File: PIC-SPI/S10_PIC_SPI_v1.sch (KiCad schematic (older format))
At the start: 175 parts, among them P1 M25P80 ISP, P10 CONN_4, P19 XILINX CABLE2, P2 CONN_4, P3 CONN_2, P4 S100_MALE, P5 PIC_ISP, P6 CONN_1, P7 CONN_1, P8 CONN_2, P9 CONN_2, Q1 ^^NPN-SOT23, Q2 ^^NPN-SOT23, Q9 ^^NPN-SOT23, SW1 RESET, SW2 RESET, SW4 FLASH_SELECT, SW50 FLASH/RUN, U1 LDO_REG_7805, U12 ^^74LV244, U14 M25P80, U15 M25P80, U16 M25P80, U17 M25P80, U18 CH341A, U19 ^^74LS541, U2 LM1086CS, U20 XC95288XL-TQ144, U3din1 ^^74HC541, U3dout1 ^^74HC541, U4 ^^74LS541, U5 ^^74LS541, U6 ^^74LS541, U8 PIC18F1330, X1 12MHz

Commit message: PIC-SPI: annotate, add 7-segment displays (2x 74HC4511), read netlist into the PCB
Source: S100 PIC_SPI_v1/backups/06-01-2016 1810
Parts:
- removed BAR? (x2): DOT-BAR, 20dip300, symbol DOT-BAR
- removed D6: DONE, symbol LED
- removed IC? (x4), U? (x2): 74LS06N, 14dip300, symbol 74LS06N
- removed JP5: JUMPER, PIN_ARRAY_2X1, symbol JUMPER
- removed P3: CONN_2, ~, symbol CONN_2
- removed P?: MCP_1_2, symbol CONN_10X2
- removed P?: CONN_6, SIL-6, symbol CONN_6
- removed P?: CONN_3, SIL-3, symbol CONN_3
- removed Q9: ^^NPN-SOT23, ~, symbol ^^NPN-SOT23
- removed R45, R?: 330, symbol R
- removed R47: 470, symbol R
- removed RR?: 220, r_pack9, symbol RR9
- removed RR?: 4700, r_pack9, symbol RR9
- removed RR?: 470, r_pack9, symbol RR9
- removed RR?: 1000, r_pack9, symbol RR9
- removed SW4: FLASH_SELECT, symbol SW_PUSH
- removed U? (x2): 74LS20, 14dip300, symbol 74LS20
- removed U? (x2): 74LS14, 14dip300, symbol 74LS14
- removed U? (x2): 74LS08, 14dip300, symbol 74LS08
- removed U? (x8): 74LS32, 14dip300, symbol 74LS32
- added BAT1: CR2032, ~, symbol BATTERY
- added C13: 0.01 uF, symbol C
- added C16, C22, C23, C24, C29, C30, C31, C32, C41, C42, C43: 0.1 uF, symbol C
- added P11: CONN_3X2, ~, symbol CONN_3X2
- added P13: MCP_1, symbol CONN_10
- added P14: MCP_2, symbol CONN_10
- added R31, R32, R33, R34, R35, R36, R37, R38, R39, R40, R41, R42, R43, R44, R6: 1K, symbol R
- added S1, S2: 7SEGM, ~, symbol 7SEGM
- added U27, U28: 74HC4511, symbol 74HC4511
- added unit 2 of U30
- added unit 3 of U30
- D10: value FLASH_1 -> D1
- D11: value FLASH_2 -> D4
- D12: value FLASH_3 -> D5
- D2: value P55 -> D2
- D3: value P54 -> D3
- D9: value FLASH_0 -> D0
- R11: value 10k -> 1K
- U2: footprint (none) -> ~
- gave numbers to parts that had none: 26
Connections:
- net labels added: 7SEG_0_D0, 7SEG_0_D1, 7SEG_0_D2, 7SEG_0_D3, 7SEG_1_D0, 7SEG_1_D1, 7SEG_1_D2, 7SEG_1_D3, BOARD_INTERRUPT_VECTb, LED_D0, LED_D1, LED_D4, LED_D5, in8259CS*, out8259CS*, out8259CS*bufferedViaU31, sXTRQ*b
- net labels removed: BOARD_INTERRUPT_VECTc, CLK, CPLD_110, CPLD_111, CPLD_112, CPLD_113, CPLD_115, CPLD_116, CPLD_117, CPLD_118, CPLD_119, CPLD_120, CPLD_121, CPLD_124, CPLD_125, CPLD_126, CPLD_128, CPLD_129, CPLD_23, CPLD_4, CPLD_5, CPLD_66, CPLD_68, CPLD_70, CPLD_71, CPLD_72, CPLD_74, CPLD_75, CPLD_76, CPLD_77, CPLD_78, CPLD_81, FLASH_0, FLASH_1, FLASH_2, FLASH_3, MCP1_CS, MCP2_CS, PU1K-A, PU1K-AA, PU1K-B, PU1K-BB, PU1K-C, PU1K-CC, PU1K-D, PU1K-DD, PU1K-E, PU1K-EE, PU1K-F, PU1K-FF, PU1K-G, PU1K-GG, PU1K-H, PU1K-HH, PU1K-I, PU1K-II, PU1K-J, PU1K-JJ, PU1K-K, PU1K-L, PU1K-M, PU1K-N, PU1K-O, PU1K-P, PU1K-Q, PU1K-R, PU1K-S, PU1K-T, PU1K-U, PU1K-V, PU1K-W, PU1K-X, PU1K-Y, PU1K-Z, SPI_S0, SPI_SCK, SPI_SEL_0, SPI_SEL_1, SPI_SEL_2, SPI_SEL_3, SPI_SI, bA1, bA2, bA3, bA4, bA5, bA6, bA7
- wire segments 1313 -> 1268
- no-connect marks 47 -> 21
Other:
- note added: "8259 PIC"
- note added: "Active Low \npDBIN*b (READ STROBE)"
- note added: "Toshiba TC74HC4511AF(F), Decoder, Driver, Non-Inverting, 2 → 6 V, 16-Pin SOP\nRS Stock No.541-9320\n"
- note added: "to CPLD"
- note added: "to MCP2308 #1"
- note added: "to MCP2308 #2"
- note added: "to RTC DS1305"
- note removed: "/WAIT is output from slave to Processor"
- note removed: "ALL TMA lines are high when Z80 \nis Bus master"
- note removed: "Active High (All TMA lines High)\n"
- note removed: "Active High (SINTA and Read and All TMA Lines high (Z80))\n"
- note removed: "Active High (SINTA and Read)\n"
- note removed: "Active Low - pDBIN**b"
- note removed: "Active Low - pDBIN*b"
- note removed: "Active Low - sINTA*b"
- note removed: "Active Low \nAddress input with I/O req"
- note removed: "Active Low\nThis board data output, CPU data input"
- note removed: "DONE"
- note removed: "Input - from U35"
- note removed: "Pin 72 (controld run/WAIT state of processor) Input"
- note removed: "SPARES"
- note removed: "WAIT to PIN 72 S100"
- note removed: "to FPGA"
- note removed: "to LED D2"
- note removed: "to LED D3"
- note removed: "to LED's"
- note removed: "to U13"
- note removed: "to U35"
- note removed: "to U36"
- note removed: "to U37"
- note removed: "to U42"
- note removed: "to U44"
- note removed: "xxxx"
- moved on the sheet: C1, C11, C12, C14, C17, C2, C20, C21, C25, C27, C28, C3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

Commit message: PIC-SPI: add CPLD I/O header P2 and EXT SPI header P3, drop debug LEDs; placement
Source: S100 PIC_SPI_v1/backups/07-01-2016 1914
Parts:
- removed D10: D1, symbol LED
- removed D11: D4, symbol LED
- removed D12: D5, symbol LED
- removed D2: D2, symbol LED
- removed D3: D3, symbol LED
- removed P10, P2: CONN_4, symbol CONN_4
- removed R13, R16, R22, R23, R24: 330, symbol R
- added P2: CONN_8X2, symbol CONN_8X2
- added P3: EXT SPI, ~, symbol CONN_4X2
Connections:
- net labels added: CPLD_110, CPLD_111, CPLD_112, CPLD_113, CPLD_115, CPLD_116, CPLD_68, CPLD_71, CPLD_74, CPLD_75, CPLD_76, CPLD_77, CPLD_78, Vbat
- net labels removed: LED_D0, LED_D1, LED_D2, LED_D3, LED_D4, LED_D5
- wire segments 1268 -> 1271
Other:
- note added: "to EXTERNAL SPI header"
- note removed: "from U7b"
- note removed: "to U"
- moved on the sheet: C22, C30, C32

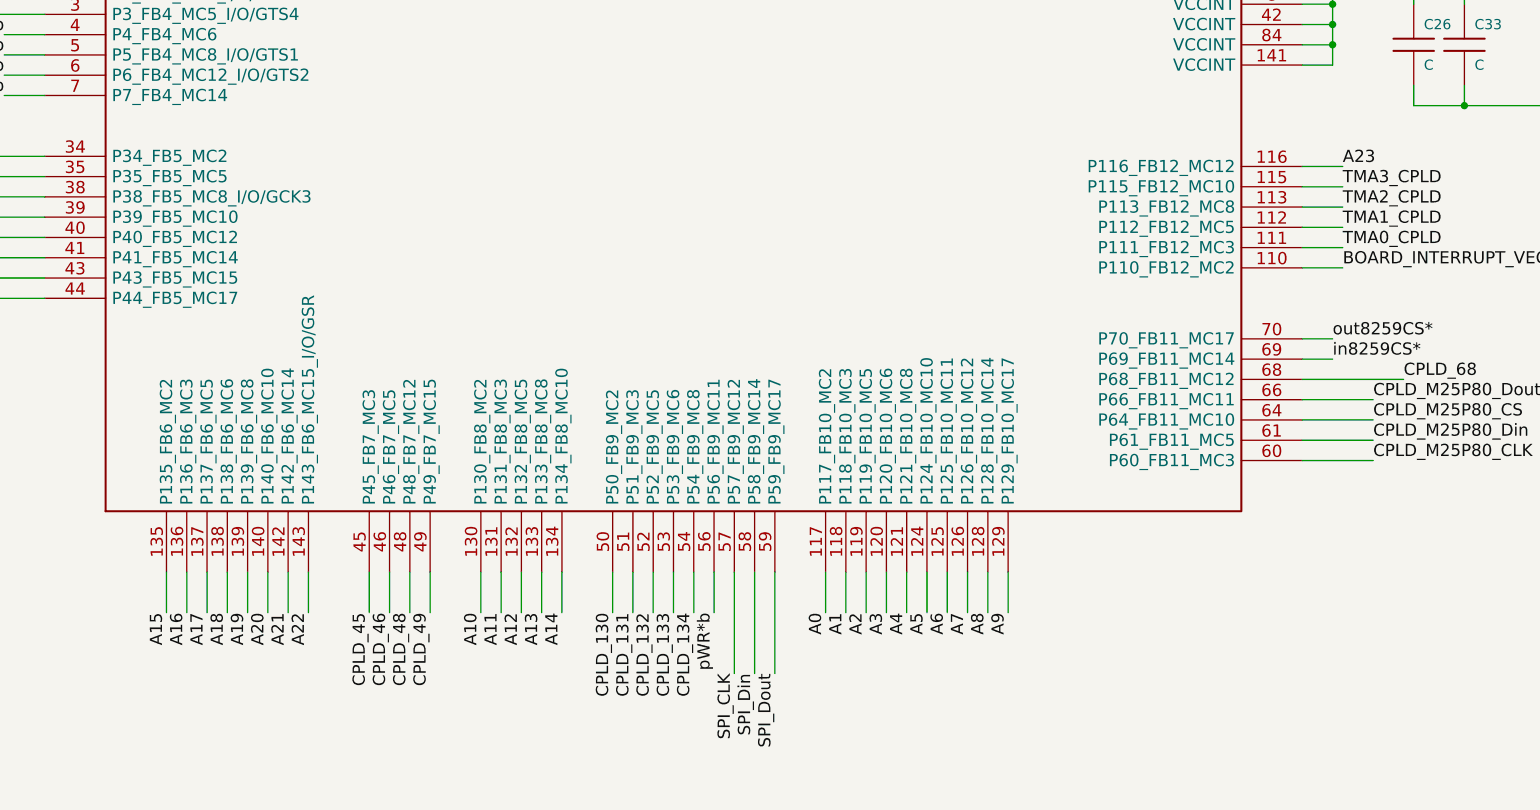
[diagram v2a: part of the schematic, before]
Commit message: PIC-SPI: rip up tracks for a reroute
Source: S100 PIC_SPI_v1/backups/09-01-2016 1434 reroute
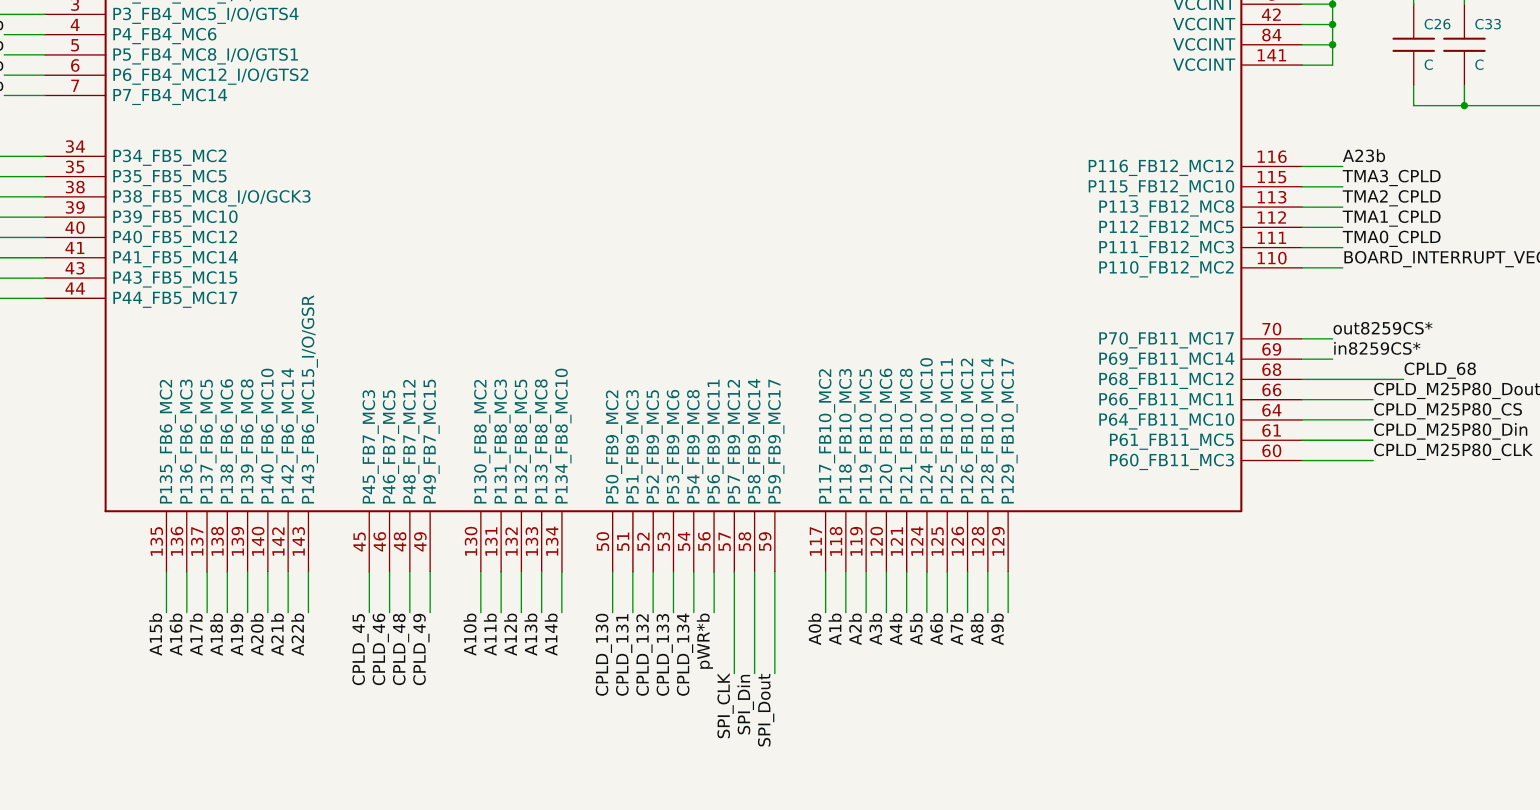
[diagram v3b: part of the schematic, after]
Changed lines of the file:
@@
 Sheet 1 1
 Title "noname.sch"
-Date "7 jan 2016"
+Date "9 jan 2016"
 Rev ""
 Comp ""
@@
 	1    0    0    -1
 $EndComp
-Text Label 30600 26550 3    60   ~ 0
-A0
-Text Label 30700 26550 3    60   ~ 0
-A1
-Text Label 30800 26550 3    60   ~ 0
-A2
-Text Label 30900 26550 3    60   ~ 0
-A3
-Text Label 31000 26550 3    60   ~ 0
-A4
-Text Label 31100 26550 3    60   ~ 0
-A5
-Text Label 31200 26550 3    60   ~ 0
-A6
-Text Label 31300 26550 3    60   ~ 0
-A7
-Text Label 31400 26550 3    60   ~ 0
-A8
-Text Label 31500 26550 3    60   ~ 0
-A9
-Text Label 28900 26550 3    60   ~ 0
-A10
-Text Label 29000 26550 3    60   ~ 0
-A11
-Text Label 29100 26550 3    60   ~ 0
-A12
-Text Label 29200 26550 3    60   ~ 0
-A13
-Text Label 29300 26550 3    60   ~ 0
-A14
-Text Label 27350 26550 3    60   ~ 0
-A15
 Text Label 33200 22350 0    60   ~ 0
 GND
@@
 Text Label 26250 20750 2    60   ~ 0
 DBUSOUT_EN
-Text Label 27650 26550 3    60   ~ 0
-A18
-Text Label 27550 26550 3    60   ~ 0
-A17
-Text Label 27450 26550 3    60   ~ 0
-A16
-Text Label 27750 26550 3    60   ~ 0
-A19
-Text Label 27850 26550 3    60   ~ 0
-A20
-Text Label 27950 26550 3    60   ~ 0
-A21
-Text Label 28050 26550 3    60   ~ 0
-A22
-Text Label 33150 24350 0    60   ~ 0
-A23
 Wire Wire Line
 	27450 26550 27450 26350
@@
 Wire Wire Line
 	32950 25800 33300 25800
+Text Label 27550 26550 3    60   ~ 0
+A17b
+Text Label 27450 26550 3    60   ~ 0
+A16b
+Text Label 27650 26550 3    60   ~ 0
+A18b
+Text Label 28900 26550 3    60   ~ 0
+A10b
+Text Label 31500 26550 3    60   ~ 0
+A9b
+Text Label 29100 26550 3    60   ~ 0
+A12b
+Text Label 27350 26550 3    60   ~ 0
+A15b
+Text Label 30900 26550 3    60   ~ 0
+A3b
+Text Label 31000 26550 3    60   ~ 0
+A4b
+Text Label 31100 26550 3    60   ~ 0
+A5b
+Text Label 29000 26550 3    60   ~ 0
+A11b
+Text Label 29300 26550 3    60   ~ 0
+A14b
+Text Label 29200 26550 3    60   ~ 0
+A13b
+Text Label 31400 26550 3    60   ~ 0
+A8b
+Text Label 31300 26550 3    60   ~ 0
+A7b
+Text Label 31200 26550 3    60   ~ 0
+A6b
+Text Label 30800 26550 3    60   ~ 0
+A2b
+Text Label 30700 26550 3    60   ~ 0
+A1b
+Text Label 30600 26550 3    60   ~ 0
+A0b
+Text Label 27750 26550 3    60   ~ 0
+A19b
+Text Label 27850 26550 3    60   ~ 0
+A20b
+Text Label 27950 26550 3    60   ~ 0
+A21b
+Text Label 28050 26550 3    60   ~ 0
+A22b
+Text Label 33150 24350 0    60   ~ 0
+A23b
 $EndSCHEMATC

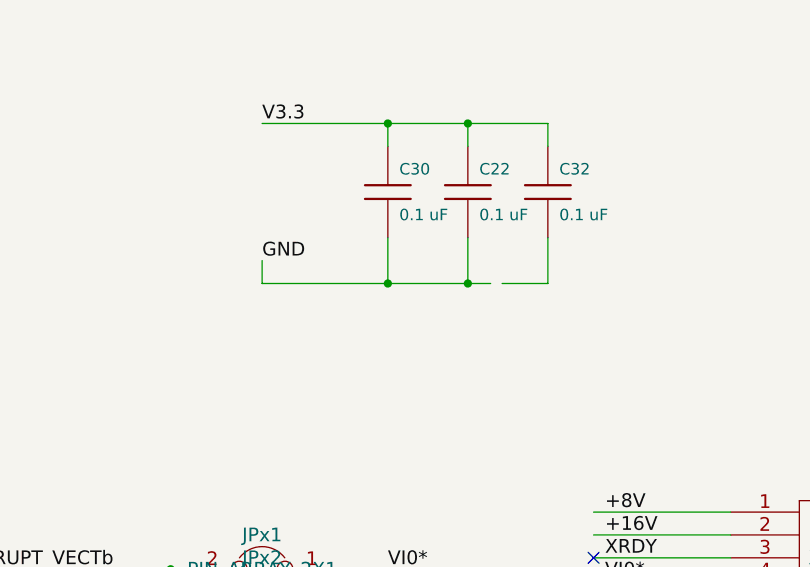
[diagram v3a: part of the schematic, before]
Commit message: PIC-SPI: schematic wiring fix, pre-route tracks before autorouting
Source: S100 PIC_SPI_v1/backups/09-01-2016 1545
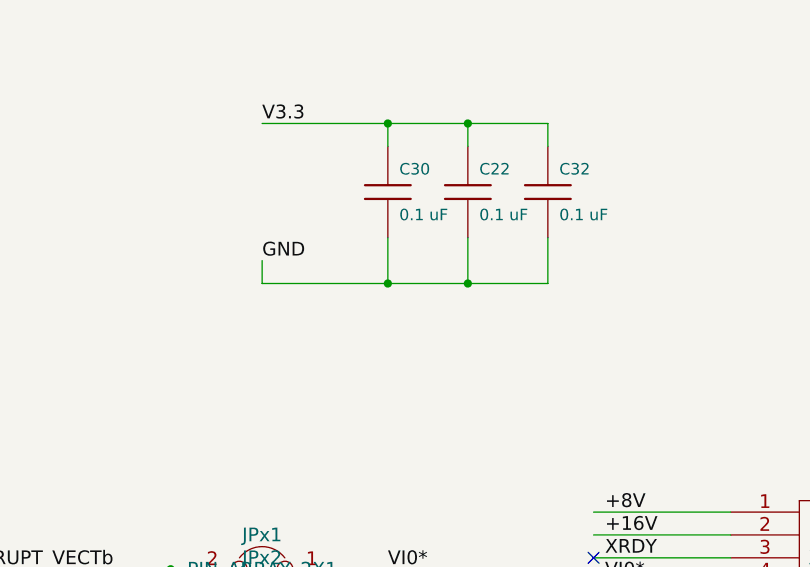
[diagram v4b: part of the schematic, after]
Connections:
- wire segments 1271 -> 1270
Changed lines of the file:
@@
 	41900 19350 41900 19450
 Wire Wire Line
-	41900 19450 42900 19450
+	41900 19450 43150 19450
 Wire Wire Line
 	42800 19250 42800 19450
@@
 Connection ~ 42800 18750
 Wire Wire Line
-	42950 19450 43150 19450
-Wire Wire Line
 	43150 19450 43150 19250
